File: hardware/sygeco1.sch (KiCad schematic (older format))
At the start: 20 parts, among them J1 SSD1306_module, J2 AVR-ISP-6, SW1 SW_Push_DPDT, SW2 SW_Push_DPDT, U1 ATtiny85-20PU

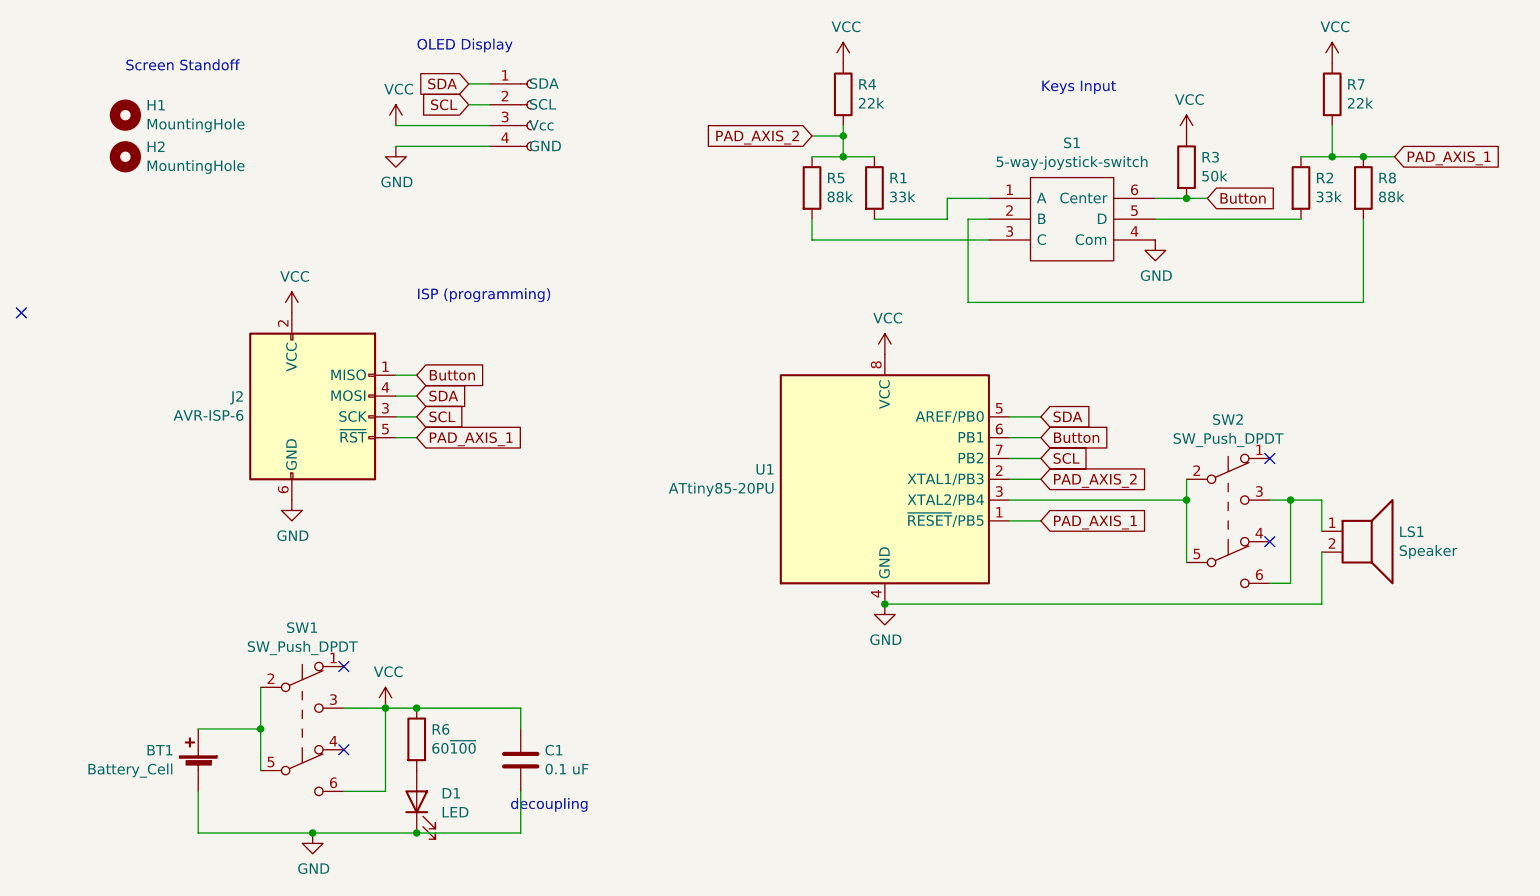
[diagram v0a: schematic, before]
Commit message: Add a led to provide feedback about whether the sound is enable or not.
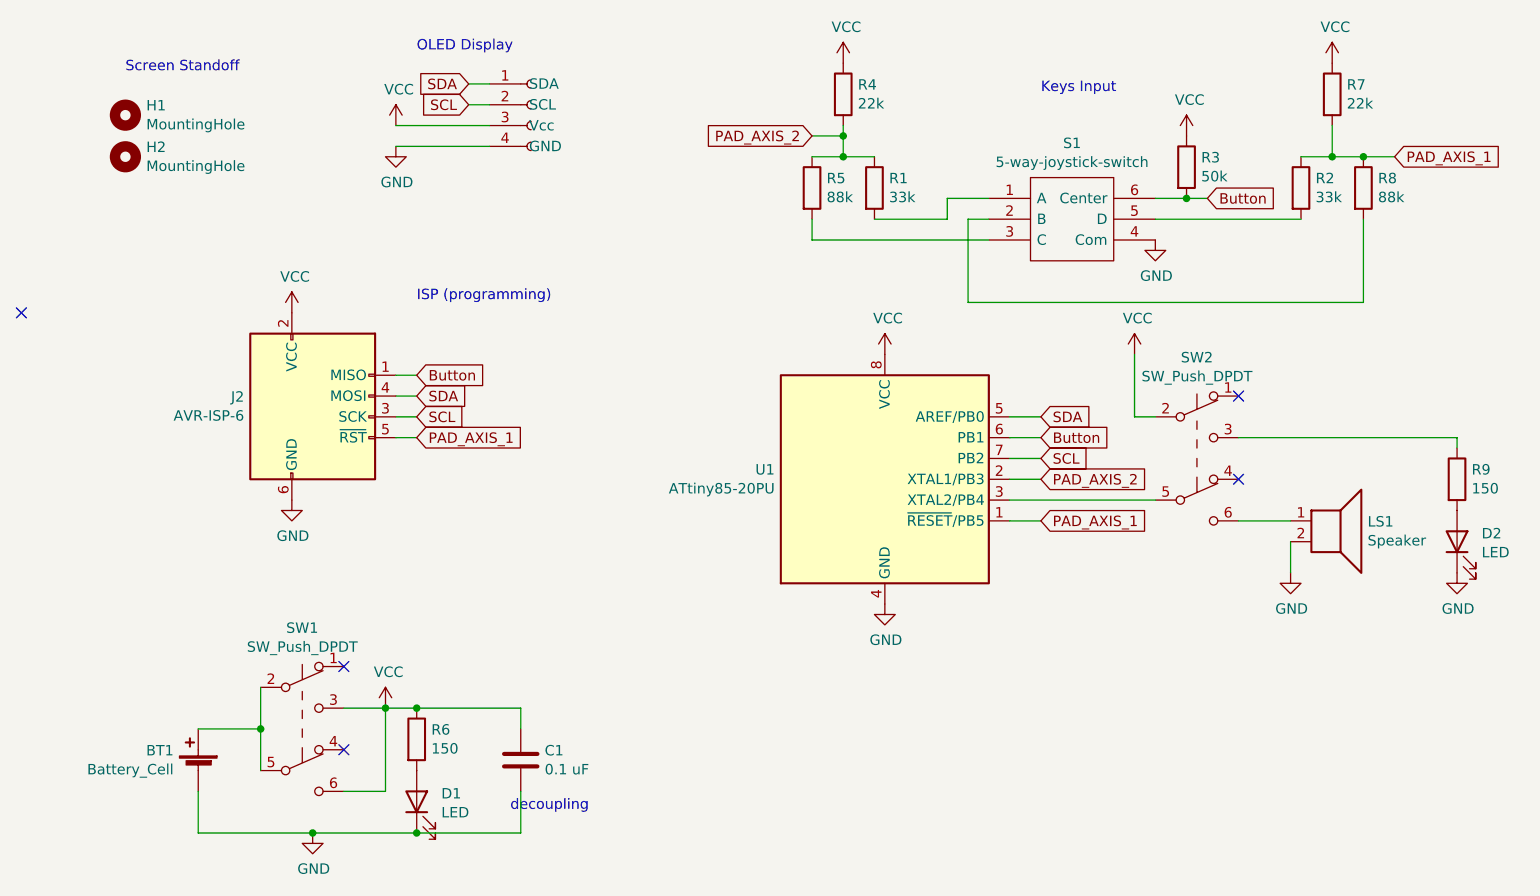
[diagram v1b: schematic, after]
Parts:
- added D2: LED, LED_SMD:LED_1206_3216Metric, symbol Device:LED
- added R9: 150, Resistor_SMD:R_1206_3216Metric_Pad1.30x1.75mm_HandSolder, symbol Device:R
- R6: value 60~100 -> 150
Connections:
- net GND: now also D2.1 (K)
- net VCC: now also SW2.2 (B)
- net at SW2.5 (B), U1.3 (XTAL2/PB4): no longer SW2.2 (B)
- net at LS1.1, SW2.6 (C): no longer SW2.3 (C)
- new net: R9.1, SW2.3 (C)
- new net: D2.2 (A), R9.2
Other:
- moved on the sheet: LS1, SW2

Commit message: Add a resistor to lower the level of buzzer (especially when using li-ion battery, with higher voltage) + fixes leds resistors.
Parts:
- added R10: 220, Resistor_SMD:R_1206_3216Metric_Pad1.30x1.75mm_HandSolder, symbol Device:R
- R6, R9: value 150 -> 470
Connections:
- net GND: now also R10.2; no longer LS1.2
- new net: LS1.2, R10.1
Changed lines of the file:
@@
 Text Notes 2350 950  0    50   ~ 0
 OLED Display
-Connection ~ 2350 4100
-Wire Wire Line
-	2850 4100 2350 4100
-Wire Wire Line
-	2350 4100 2200 4100
 Connection ~ 1850 4700
-Connection ~ 2350 4700
-Wire Wire Line
-	2350 4700 2850 4700
-Wire Wire Line
-	2350 4700 1850 4700
-$Comp
-L Device:LED D1
-U 1 1 5FA7AC0D
-P 2350 4550
-F 0 "D1" V 2389 4432 50  0000 R CNN
-F 1 "LED" V 2298 4432 50  0000 R CNN
-F 2 "LED_SMD:LED_1206_3216Metric" H 2350 4550 50  0001 C CNN
-F 3 "~" H 2350 4550 50  0001 C CNN
-	1    2350 4550
-	0    -1   -1   0
-$EndComp
 $Comp
 L Device:LED D2
@@
 P 7350 3000
 F 0 "R9" H 7420 3046 50  0000 L CNN
-F 1 "150" H 7420 2955 50  0000 L CNN
+F 1 "470" H 7420 2955 50  0000 L CNN
 F 2 "Resistor_SMD:R_1206_3216Metric_Pad1.30x1.75mm_HandSolder" V 7280 3000 50  0001 C CNN
 F 3 "~" H 7350 3000 50  0001 C CNN
@@
 $EndComp
 $Comp
-L Device:R R6
-U 1 1 5FA79D6B
-P 2350 4250
-F 0 "R6" H 2420 4296 50  0000 L CNN
-F 1 "150" H 2420 4205 50  0000 L CNN
-F 2 "Resistor_SMD:R_1206_3216Metric_Pad1.30x1.75mm_HandSolder" V 2280 4250 50  0001 C CNN
-F 3 "~" H 2350 4250 50  0001 C CNN
-	1    2350 4250
-	1    0    0    -1
-$EndComp
-$Comp
 L power:GND #PWR0104
 U 1 1 5FE29128
-P 6550 3450
-F 0 "#PWR0104" H 6550 3200 50  0001 C CNN
-F 1 "GND" H 6555 3277 50  0000 C CNN
-F 2 "" H 6550 3450 50  0001 C CNN
-F 3 "" H 6550 3450 50  0001 C CNN
-	1    6550 3450
+P 6550 3750
+F 0 "#PWR0104" H 6550 3500 50  0001 C CNN
+F 1 "GND" H 6555 3577 50  0000 C CNN
+F 2 "" H 6550 3750 50  0001 C CNN
+F 3 "" H 6550 3750 50  0001 C CNN
+	1    6550 3750
 	1    0    0    -1
 $EndComp
@@
 Wire Wire Line
 	5800 2700 5900 2700
+Wire Wire Line
+	2350 4700 1850 4700
+Wire Wire Line
+	2350 4700 2850 4700
+Connection ~ 2350 4700
+$Comp
+L Device:LED D1
+U 1 1 5FA7AC0D
+P 2350 4550
+F 0 "D1" V 2389 4432 50  0000 R CNN
+F 1 "LED" V 2298 4432 50  0000 R CNN
+F 2 "LED_SMD:LED_1206_3216Metric" H 2350 4550 50  0001 C CNN
+F 3 "~" H 2350 4550 50  0001 C CNN
+	1    2350 4550
+	0    -1   -1   0
+$EndComp
+Wire Wire Line
+	2350 4100 2200 4100
+Wire Wire Line
+	2850 4100 2350 4100
+Connection ~ 2350 4100
+$Comp
+L Device:R R6
+U 1 1 5FA79D6B
+P 2350 4250
+F 0 "R6" H 2420 4296 50  0000 L CNN
+F 1 "470" H 2420 4205 50  0000 L CNN
+F 2 "Resistor_SMD:R_1206_3216Metric_Pad1.30x1.75mm_HandSolder" V 2280 4250 50  0001 C CNN
+F 3 "~" H 2350 4250 50  0001 C CNN
+	1    2350 4250
+	1    0    0    -1
+$EndComp
+$Comp
+L Device:R R10
+U 1 1 5FE5BFCE
+P 6550 3600
+F 0 "R10" H 6620 3646 50  0000 L CNN
+F 1 "220" H 6620 3555 50  0000 L CNN
+F 2 "Resistor_SMD:R_1206_3216Metric_Pad1.30x1.75mm_HandSolder" V 6480 3600 50  0001 C CNN
+F 3 "~" H 6550 3600 50  0001 C CNN
+	1    6550 3600
+	1    0    0    -1
+$EndComp
 $EndSCHEMATC

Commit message: cleaning
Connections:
- net GND: now also LS1.2; no longer R10.2
- net at LS1.1: now also R10.1; no longer SW2.6 (C)
- new net: R10.2, SW2.6 (C)
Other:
- moved on the sheet: LS1, R10
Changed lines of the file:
@@
 Title "Sygeco 1"
 Date ""
-Rev "0.1"
+Rev "0.2"
 Comp "Sylphide Consulting"
 Comment1 ""
@@
 L Device:Speaker LS1
 U 1 1 5FA28788
-P 6750 3200
-F 0 "LS1" H 6920 3196 50  0000 L CNN
-F 1 "Speaker" H 6920 3105 50  0000 L CNN
-F 2 "Buzzer_Beeper:MagneticBuzzer_ProSignal_ABT-410-RC" H 6750 3000 50  0001 C CNN
-F 3 "~" H 6740 3150 50  0001 C CNN
-	1    6750 3200
+P 6800 3200
+F 0 "LS1" H 6970 3196 50  0000 L CNN
+F 1 "Speaker" H 6970 3105 50  0000 L CNN
+F 2 "Buzzer_Beeper:MagneticBuzzer_ProSignal_ABT-410-RC" H 6800 3000 50  0001 C CNN
+F 3 "~" H 6790 3150 50  0001 C CNN
+	1    6800 3200
 	1    0    0    -1
 $EndComp
@@
 L power:GND #PWR0104
 U 1 1 5FE29128
-P 6550 3750
-F 0 "#PWR0104" H 6550 3500 50  0001 C CNN
-F 1 "GND" H 6555 3577 50  0000 C CNN
-F 2 "" H 6550 3750 50  0001 C CNN
-F 3 "" H 6550 3750 50  0001 C CNN
-	1    6550 3750
-	1    0    0    -1
-$EndComp
-Wire Wire Line
-	6550 3450 6550 3300
-Wire Wire Line
-	6300 3200 6550 3200
+P 6600 3500
+F 0 "#PWR0104" H 6600 3250 50  0001 C CNN
+F 1 "GND" H 6605 3327 50  0000 C CNN
+F 2 "" H 6600 3500 50  0001 C CNN
+F 3 "" H 6600 3500 50  0001 C CNN
+	1    6600 3500
+	1    0    0    -1
+$EndComp
 Wire Wire Line
 	6300 2800 7350 2800
@@
 L Device:R R10
 U 1 1 5FE5BFCE
-P 6550 3600
-F 0 "R10" H 6620 3646 50  0000 L CNN
-F 1 "220" H 6620 3555 50  0000 L CNN
-F 2 "Resistor_SMD:R_1206_3216Metric_Pad1.30x1.75mm_HandSolder" V 6480 3600 50  0001 C CNN
-F 3 "~" H 6550 3600 50  0001 C CNN
-	1    6550 3600
-	1    0    0    -1
-$EndComp
+P 6450 3200
+F 0 "R10" H 6520 3246 50  0000 L CNN
+F 1 "220" H 6520 3155 50  0000 L CNN
+F 2 "Resistor_SMD:R_1206_3216Metric_Pad1.30x1.75mm_HandSolder" V 6380 3200 50  0001 C CNN
+F 3 "~" H 6450 3200 50  0001 C CNN
+	1    6450 3200
+	0    1    1    0
+$EndComp
+Wire Wire Line
+	6600 3500 6600 3300
 $EndSCHEMATC

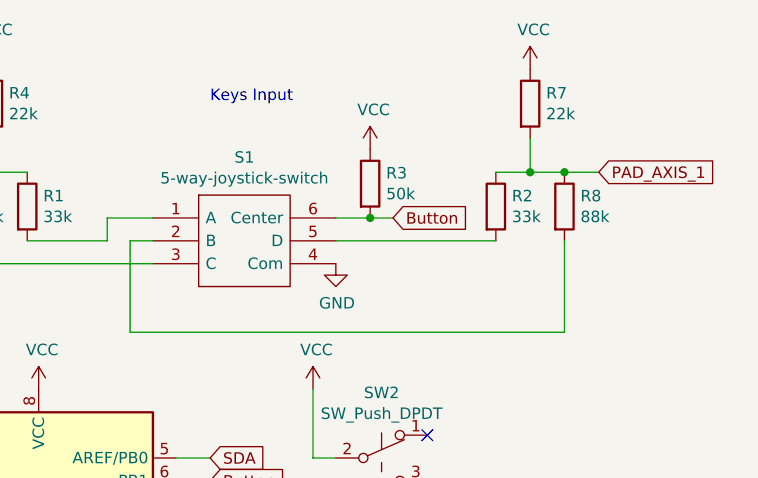
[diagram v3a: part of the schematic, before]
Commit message: final touch + generates files for pcb production
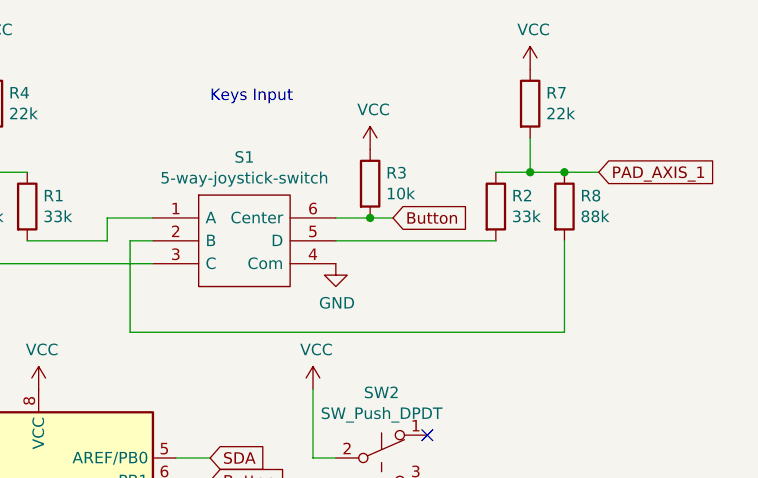
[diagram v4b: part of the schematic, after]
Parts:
- R3: value 50k -> 10k
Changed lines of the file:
@@
 P 6050 1500
 F 0 "R3" H 6120 1546 50  0000 L CNN
-F 1 "50k" H 6120 1455 50  0000 L CNN
+F 1 "10k" H 6120 1455 50  0000 L CNN
 F 2 "Resistor_SMD:R_1206_3216Metric_Pad1.30x1.75mm_HandSolder" V 5980 1500 50  0001 C CNN
 F 3 "~" H 6050 1500 50  0001 C CNN
